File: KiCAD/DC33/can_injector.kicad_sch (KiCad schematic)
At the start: 27 parts, among them U17 ADG849YKSZ-REEL, U19 ADG849YKSZ-REEL, U21 ALM2403QPWPRQ1, U22 TMUX1108PWR, U24 TMUX1108PWR, U27 TPS22810TDBVRQ1

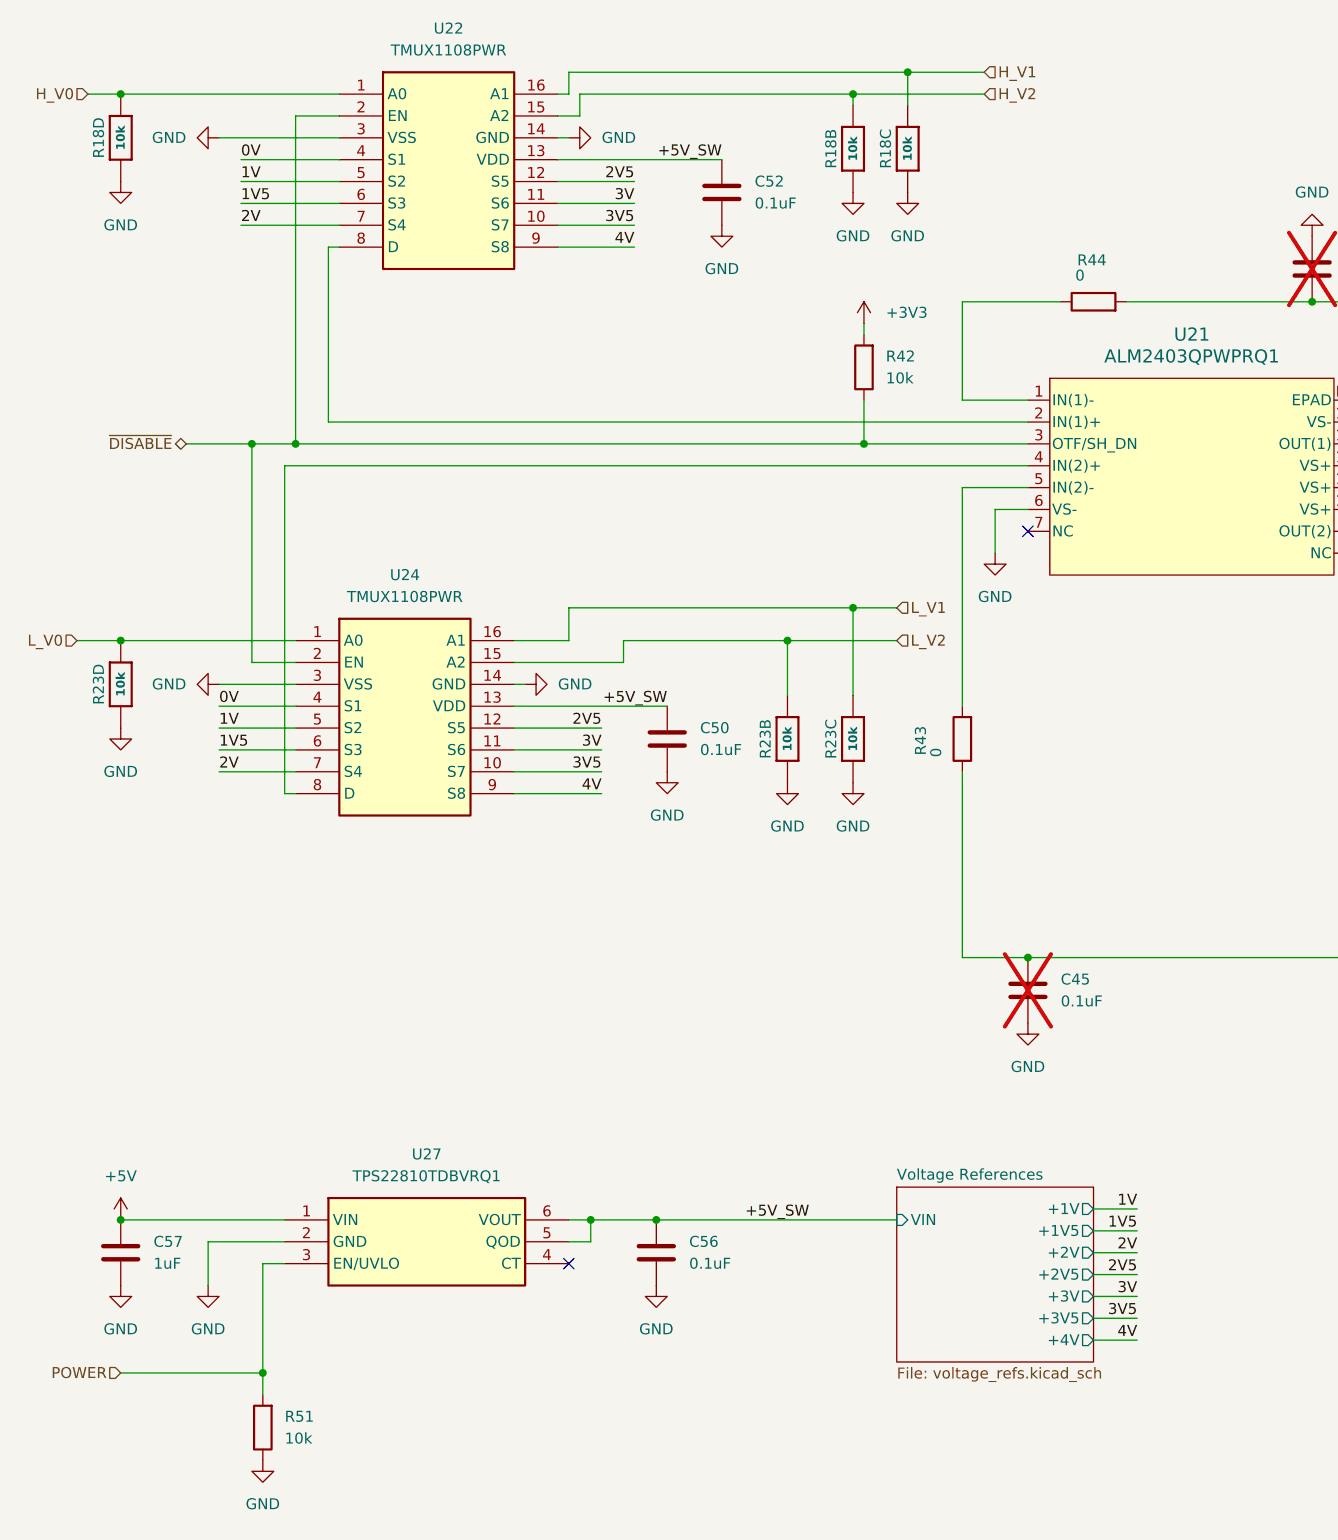
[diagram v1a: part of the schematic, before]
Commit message: schematic fixes R-2R DAC
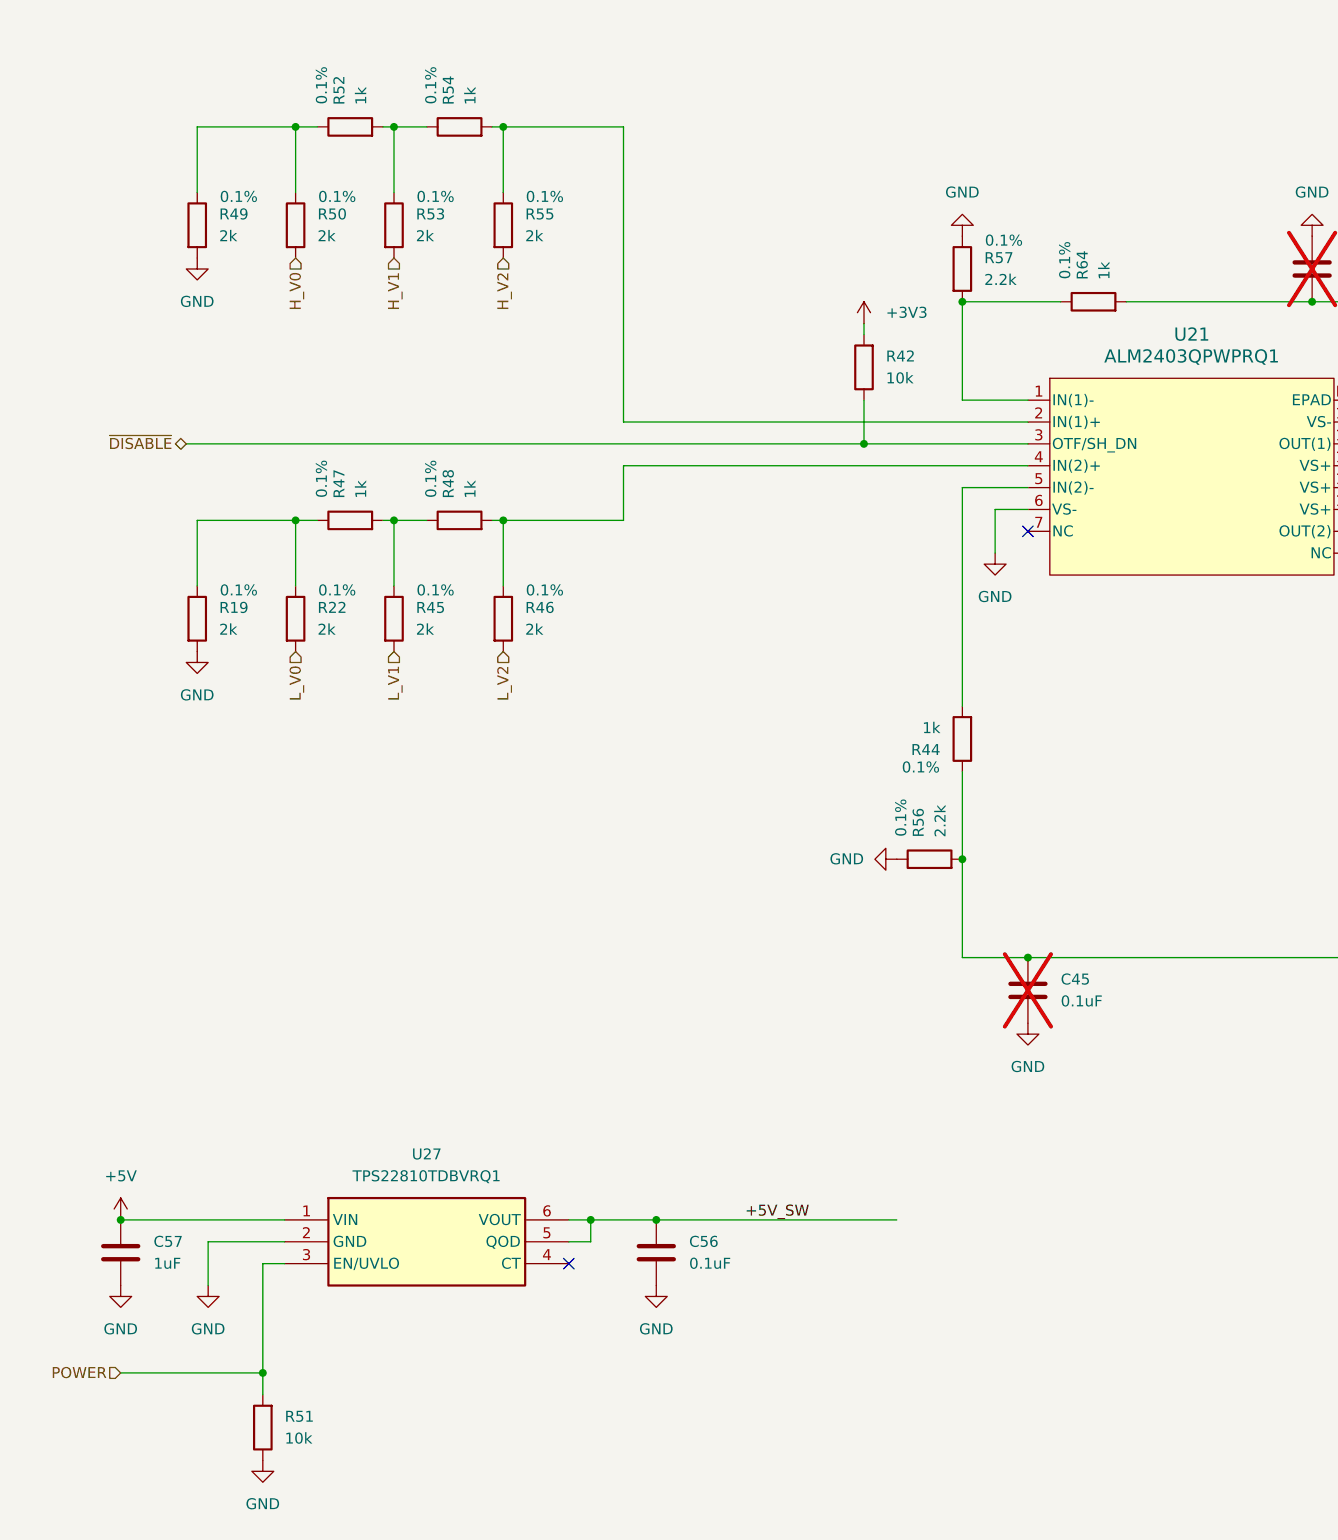
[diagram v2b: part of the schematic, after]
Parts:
- removed C50, C52: 0.1uF, Capacitor_SMD:C_0603_1608Metric, symbol Library:C
- removed unit 3 of R18
- removed unit 4 of R18
- removed unit 2 of R18
- removed unit 3 of R23
- removed unit 2 of R23
- removed unit 4 of R23
- removed R43: 0, Resistor_SMD:R_0603_1608Metric, symbol Library:R
- removed U22, U24: TMUX1108PWR, Library:SOP65P640X120-16N, symbol Library:TMUX1108PWR
- added R19, R22, R45, R46, R49, R50, R53, R55: 2k, Resistor_SMD:R_0603_1608Metric, symbol Library:R
- added R47, R48, R52, R54, R64: 1k, Resistor_SMD:R_0603_1608Metric, symbol Library:R
- added R56, R57: 2.2k, Resistor_SMD:R_0603_1608Metric, symbol Library:R
- R44: value 0 -> 1k; Manufacturer Panasonic Electronic Components -> Panasonic Industry; Manufacturer Part Number ERJ-3GEY0R00V -> ERA-3AEB102V; Tolerance 1% -> 0.1%
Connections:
- net GND: now also R19.2, R49.2, R56.1, R57.1
- net H_V0: now also R50.2
- net H_V1: now also R53.2
- net H_V2: now also R55.2
- net L_V0: now also R22.2
- net L_V1: now also R45.2
- net L_V2: now also R46.2
- net at C45.1, R39.2, R40.1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: now also R44.1, R56.2
- net at U21.5 (IN(2)-): now also R44.2
- net at U21.4 (IN(2)+): now also R46.1, R48.2
- net at C44.2, R38.1, R41.2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: now also R64.2; no longer R44.2
- net at U21.1 (IN(1)-): now also R57.2, R64.1; no longer R44.1
- net at U21.2 (IN(1)+): now also R54.2, R55.1
- new net: R49.1, R50.1, R52.1
- new net: R52.2, R53.1, R54.1
- new net: R19.1, R22.1, R47.1
- new net: R45.1, R47.2, R48.1
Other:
- removed sheet Voltage References

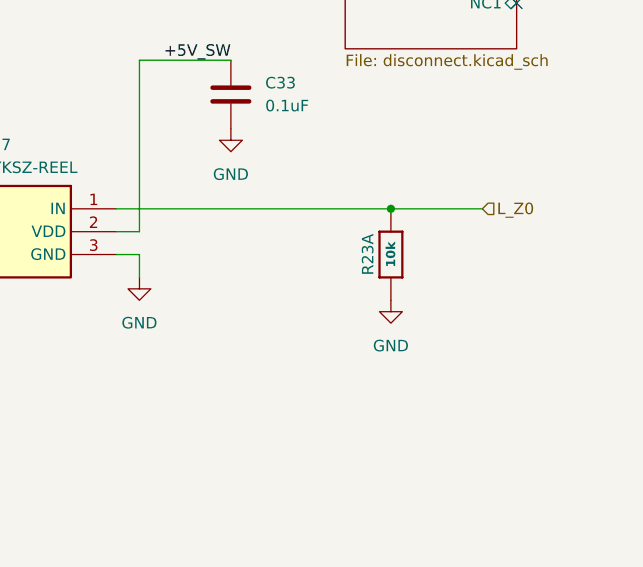
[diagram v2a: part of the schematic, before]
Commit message: Initial changes - more to do!
Updated based on the new schematic, removed a bunch of old parts. LOTS of traces need to be redone. Parts are imported. Schematic needs the switch to be matched up to the pins on the footprint. Old board shape still there. More silkscreen removed.
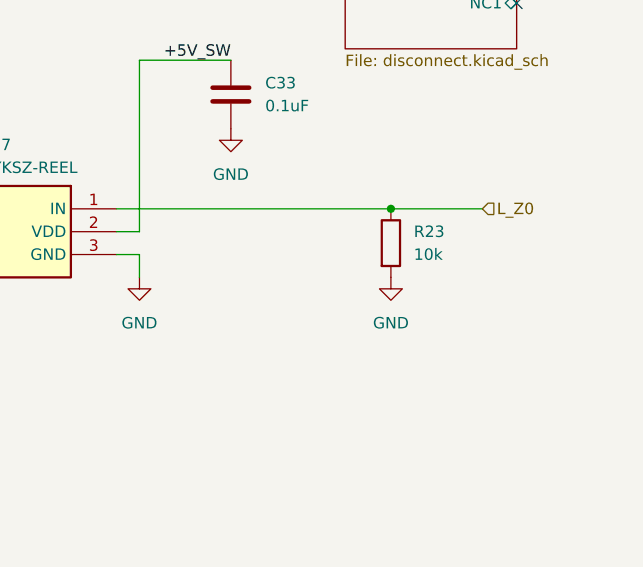
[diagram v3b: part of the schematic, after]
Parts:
- removed R23: 10k, Library:RESPACK_4X0603, symbol Library:RESISTOR_4PACK
- added R23: 10k, Resistor_SMD:R_0603_1608Metric, symbol Library:R
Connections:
- net GND: now also R23.2
- net L_Z0: now also R23.1
